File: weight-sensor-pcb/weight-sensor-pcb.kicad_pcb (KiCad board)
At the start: 2 copper layers, 60 parts, among them IC1 SN65HVD230DR, IC2 INA333AIDGKR, IC3 INA333AIDGKR, IC4 INA333AIDGKR, IC5 INA333AIDGKR, IC7 AP63203WU-7, J1 TC2030, J2 54602-908LF, J3 SM04B-GHS-TB_LF__SN_, J4 Conn_01x05_Pin, J5 SM04B-GHS-TB_LF__SN_, J6 SM04B-GHS-TB_LF__SN_, J7 SM04B-GHS-TB_LF__SN_, J8 54602-908LF, J9 10118192-0002LF, Q2 DMP3099L-7, U1 OPA333xxD, U2 OPA333xxD, U3 OPA333xxD, U4 STM32F042F4P6, U5 OPA333xxD

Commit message: layout progress 1
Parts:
- removed R25, R27: 100Ω, Capstone:RESC1608X55N
- added IC6: LM2776DBVR, Capstone:SOT95P280X145-6N, F.Cu at (18.8, 75.5)
- added R18: 0Ω, Capstone:RESC1608X55N, F.Cu at (40.4, 88.7)
- added R4: 0Ω, Capstone:RESC1608X55N, F.Cu at (36.5, 81.0)
- added TP1: VDD, TestPoint:TestPoint_Pad_D1.5mm, F.Cu at (37.0, 99.4)
- added TP10: GND, TestPoint:TestPoint_Pad_D1.5mm, F.Cu at (40.6, 113.6)
- added TP11: CAN_RX, TestPoint:TestPoint_Pad_D1.5mm, F.Cu at (25.9, 99.4)
- added TP12: CAN_TX, TestPoint:TestPoint_Pad_D1.5mm, F.Cu at (25.9, 103.0)
- added TP13: CAN_L, TestPoint:TestPoint_Pad_D1.5mm, F.Cu at (25.9, 106.5)
- added TP14: CAN_H, TestPoint:TestPoint_Pad_D1.5mm, F.Cu at (25.9, 110.0)
- added TP15: RS Mode, TestPoint:TestPoint_Pad_D1.5mm, F.Cu at (25.9, 113.6)
- added TP16: Vref, TestPoint:TestPoint_Pad_D1.5mm, F.Cu at (31.5, 99.4)
- added TP17: V1 OUT, TestPoint:TestPoint_Pad_D1.5mm, F.Cu at (31.5, 103.0)
- added TP18: V2 OUT, TestPoint:TestPoint_Pad_D1.5mm, F.Cu at (31.5, 106.5)
- added TP19: V3 OUT, TestPoint:TestPoint_Pad_D1.5mm, F.Cu at (31.5, 110.0)
- added TP2: BOOT0, TestPoint:TestPoint_Pad_D1.5mm, F.Cu at (115.0, 64.7)
- added TP20: V4 OUT, TestPoint:TestPoint_Pad_D1.5mm, F.Cu at (31.5, 113.6)
- added TP21: SW, TestPoint:TestPoint_Pad_D1.5mm, F.Cu at (104.1, 37.3)
- added TP3: NRST, TestPoint:TestPoint_Pad_D1.5mm, F.Cu at (37.0, 106.5)
- added TP4: VDD, TestPoint:TestPoint_Pad_D1.5mm, F.Cu at (37.0, 110.0)
- added TP5: VDDA, TestPoint:TestPoint_Pad_D1.5mm, F.Cu at (37.0, 113.6)
- added TP6: ADC_IN0, TestPoint:TestPoint_Pad_D1.5mm, F.Cu at (40.6, 99.4)
- added TP7: ADC_IN1, TestPoint:TestPoint_Pad_D1.5mm, F.Cu at (40.6, 103.0)
- added TP8: ADC_IN5, TestPoint:TestPoint_Pad_D1.5mm, F.Cu at (40.6, 106.5)
- added TP9: ADC_IN6, TestPoint:TestPoint_Pad_D1.5mm, F.Cu at (40.6, 110.0)
- R2, R9: value 100Ω -> 0Ω
- moved J8 83.1 mm to (43.6, 29.5), turned to 180 degrees
- moved J2 74.8 mm to (62.0, 29.5), turned to 180 degrees
- moved C13 57.8 mm to (101.0, 40.1), turned to 180 degrees
- moved IC7 55.3 mm to (99.5, 43.6), turned to -90 degrees
- moved L3 55.0 mm to (106.5, 42.6)
- moved Q2 49.5 mm to (94.5, 41.6), turned to 90 degrees
- moved R8 47.1 mm to (117.5, 65.0), turned to 180 degrees
- moved R24 43.7 mm to (94.0, 47.1), turned to 90 degrees
- moved C14 43.5 mm to (98.0, 47.6), turned to 180 degrees
- moved D2 42.8 mm to (95.0, 44.6), turned to 180 degrees
- moved C16 41.3 mm to (102.4, 50.6), turned to 180 degrees
- moved C15 41.0 mm to (102.4, 47.8), turned to 180 degrees
- moved C5 35.1 mm to (108.0, 64.0)
- moved C7 35.1 mm to (108.0, 68.0)
- moved FB1 32.0 mm to (100.9, 55.5)
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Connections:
- net /Power Supply/Input renamed /Power Supply/VIN
- net Net-(IC7-SW) renamed /Power Supply/SW
- net Net-(U1--) renamed /Force Sensor & Analog Front-End/V4out
- net Net-(U2--) renamed /Force Sensor & Analog Front-End/V1out
- net Net-(U3--) renamed /Force Sensor & Analog Front-End/V2out
- net Net-(U5--) renamed /Force Sensor & Analog Front-End/V3out
- IC2 pad 5: GND -> /Force Sensor & Analog Front-End/Vref
- IC3 pad 5: GND -> /Force Sensor & Analog Front-End/Vref
- IC4 pad 5: GND -> /Force Sensor & Analog Front-End/Vref
- IC5 pad 5: GND -> /Force Sensor & Analog Front-End/Vref
- J2 pad 3: unconnected-(J2-Pad3) -> +24V
- J2 pad 4: unconnected-(J2-Pad4) -> GND
- J2 pad 5: unconnected-(J2-Pad5) -> +24V
- J2 pad 6: unconnected-(J2-Pad6) -> GND
- J2 pad 7: unconnected-(J2-Pad7) -> +24V
- J2 pad 8: unconnected-(J2-Pad8) -> GND
- J8 pad 3: unconnected-(J8-Pad3) -> +24V
- J8 pad 4: unconnected-(J8-Pad4) -> GND
- J8 pad 5: unconnected-(J8-Pad5) -> +24V
- J8 pad 6: unconnected-(J8-Pad6) -> GND
- J8 pad 7: unconnected-(J8-Pad7) -> +24V
- J8 pad 8: unconnected-(J8-Pad8) -> GND
- R1 pad 2: Net-(R1-Pad2) -> Net-(IC4-RG_2)
- R2 pad 1: Net-(R1-Pad2) -> Net-(C1-Pad2)
- R2 pad 2: Net-(IC4-RG_2) -> /STM32 Microcontroller/ADC_IN0
- R23 pad 2: Net-(R23-Pad2) -> Net-(IC3-RG_2)
- R26 pad 2: Net-(R26-Pad2) -> Net-(IC2-RG_2)
- R3 pad 2: Net-(R3-Pad2) -> Net-(IC5-RG_2)
- R9 pad 1: Net-(R3-Pad2) -> Net-(C3-Pad2)
- R9 pad 2: Net-(IC5-RG_2) -> /STM32 Microcontroller/ADC_IN5
- U1 pad 3: GND -> /Force Sensor & Analog Front-End/Vref
- U2 pad 3: GND -> /Force Sensor & Analog Front-End/Vref
- U3 pad 3: GND -> /Force Sensor & Analog Front-End/Vref
- U5 pad 3: GND -> /Force Sensor & Analog Front-End/Vref
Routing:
- net +24V: track 0.00 -> 24.3 mm
- net +3.3V: track 1.81 -> 25.5 mm
- net /CAN Interface/CAN_L: track 0.00 -> 19.2 mm
- net /CAN Interface/CAN_H: track 0.00 -> 19.2 mm
- net /Power Supply/SW: track 0.00 -> 13.7 mm
- net /STM32 Microcontroller/NRST: track 0.00 -> 11.2 mm
- net GND: track 1.87 -> 12.3 mm, vias 0 -> 13
- net /STM32 Microcontroller/SWDIO: track 0.00 -> 10.4 mm
- net /STM32 Microcontroller/SWCLK: track 0.00 -> 7.21 mm
- net /Power Supply/VIN: track 0.00 -> 5.56 mm
- net +5V: track 0.00 -> 4.07 mm
- net /STM32 Microcontroller/BOOT0: track 0.00 -> 3.93 mm
- net Net-(IC7-BST): track 0.00 -> 2.57 mm
- net /CAN Interface/RS Mode: track 0.00 -> 1.71 mm
- net /CAN Interface/CAN_RX: track 8.68 -> 7.37 mm
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- added copper zone on F.Cu, net +3.3V
- added copper zone on F.Cu, net /Power Supply/VIN
- added copper zone on B.Cu, net GND

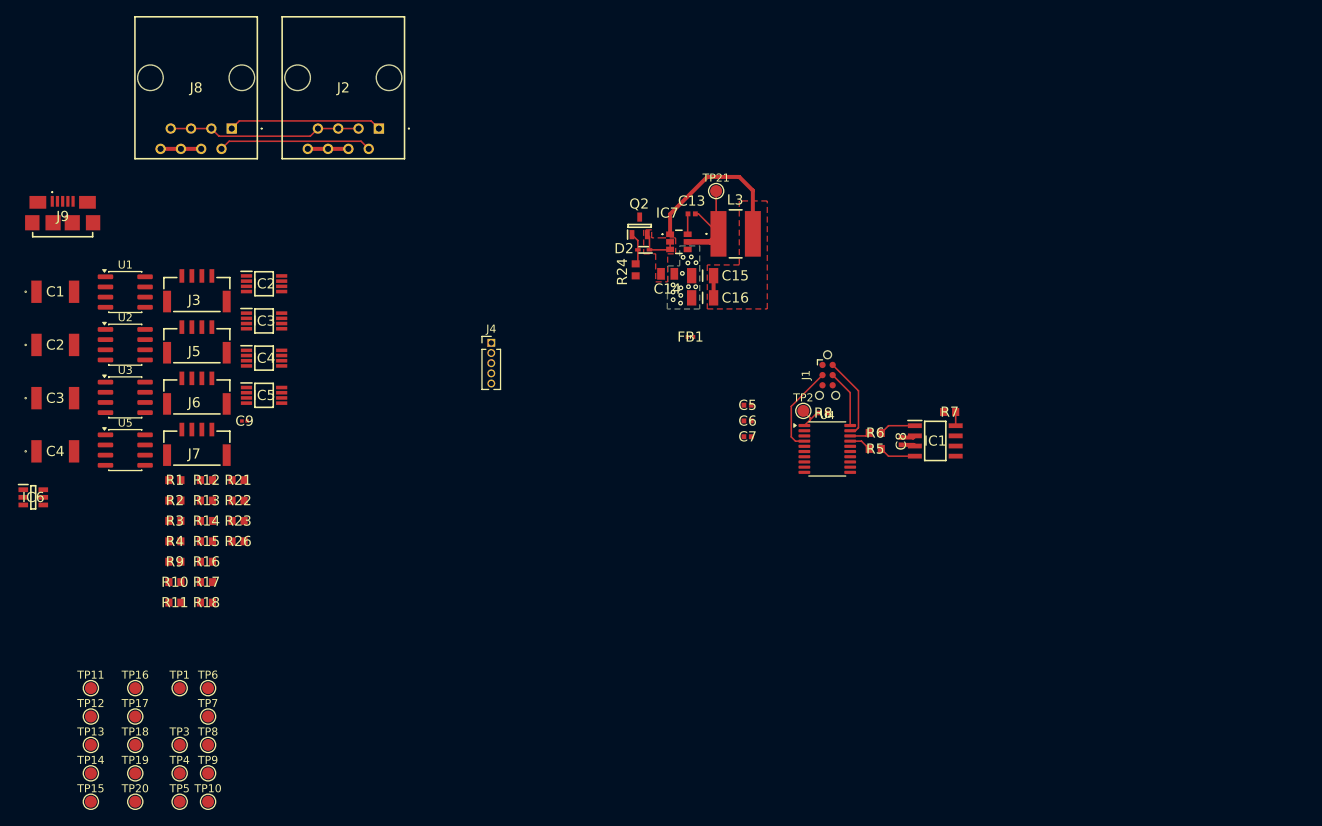
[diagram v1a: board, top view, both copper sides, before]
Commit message: more layout updates, add mounting hole pads to schematic
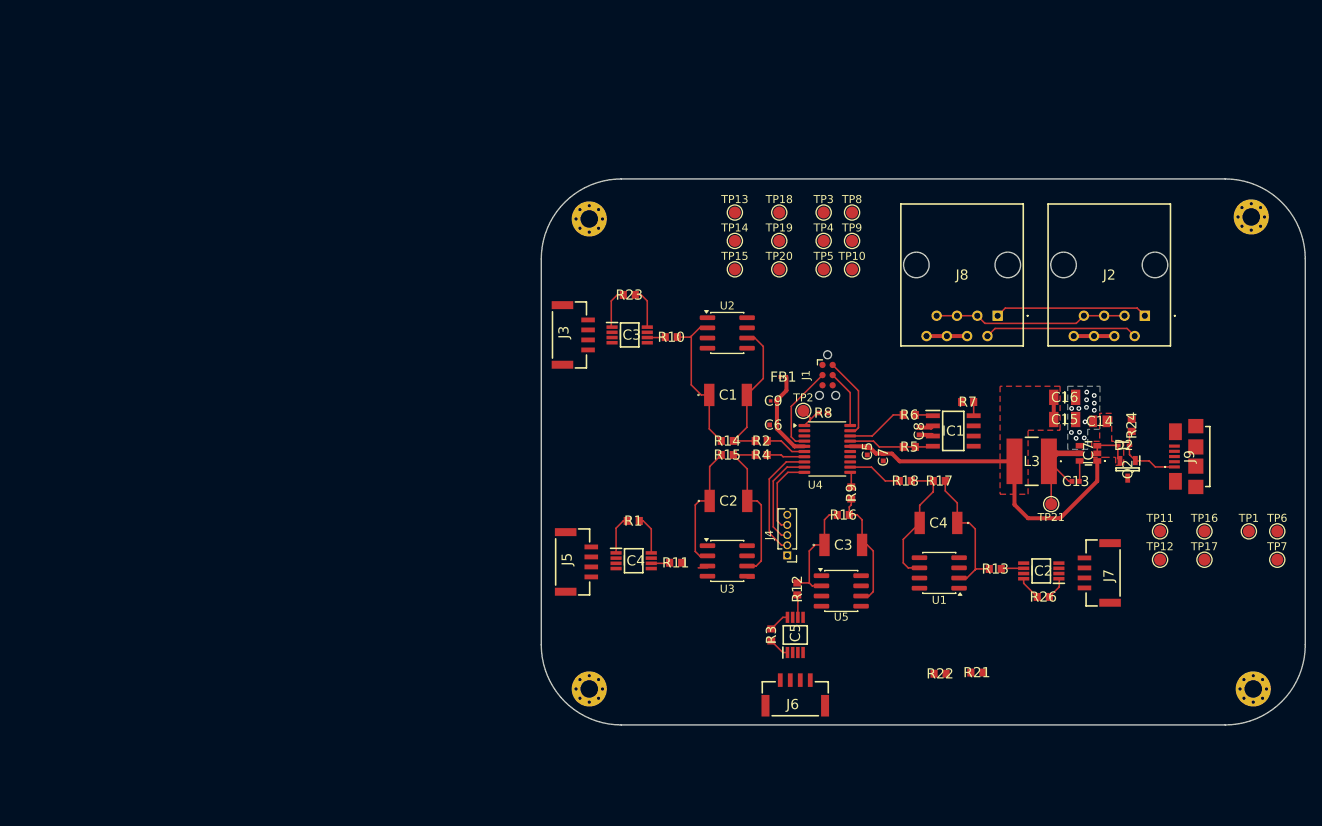
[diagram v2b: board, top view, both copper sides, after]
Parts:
- removed IC6: LM2776DBVR, Capstone:SOT95P280X145-6N
- added H1: MountingHole_Pad, MountingHole:MountingHole_2.2mm_M2_Pad_Via, F.Cu at (88.2, 40.8)
- added H2: MountingHole_Pad, MountingHole:MountingHole_2.2mm_M2_Pad_Via, F.Cu at (171.0, 40.5)
- added H3: MountingHole_Pad, MountingHole:MountingHole_2.2mm_M2_Pad_Via, F.Cu at (171.2, 99.5)
- added H4: MountingHole_Pad, MountingHole:MountingHole_2.2mm_M2_Pad_Via, F.Cu at (88.2, 99.5)
- moved J9 144.0 mm to (163.3, 70.5), turned to 90 degrees
- moved TP11 135.1 mm to (159.6, 79.8)
- moved TP12 135.1 mm to (159.6, 83.3)
- moved TP16 135.1 mm to (165.2, 79.8)
- moved TP17 135.1 mm to (165.2, 83.3)
- moved TP6 135.1 mm to (174.2, 79.8)
- moved TP7 135.1 mm to (174.2, 83.3)
- moved TP1 135.1 mm to (170.7, 79.8)
- moved J7 112.6 mm to (150.3, 85.0), turned to 90 degrees
- moved C4 110.8 mm to (131.9, 78.8), turned to 180 degrees
- moved U1 107.6 mm to (132.0, 85.0), turned to 180 degrees
- moved TP10 104.4 mm to (121.1, 47.0)
- moved TP13 104.4 mm to (106.5, 40.0)
- moved TP14 104.4 mm to (106.5, 43.5)
- moved TP15 104.4 mm to (106.5, 47.0)
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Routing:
- net +3.3V: track 25.5 -> 46.8 mm
- net Net-(C2-Pad2): track 0.00 -> 20.2 mm
- net /Force Sensor & Analog Front-End/V1out: track 0.00 -> 19.5 mm
- net Net-(C1-Pad2): track 0.00 -> 18.6 mm
- net /Force Sensor & Analog Front-End/V4out: track 0.00 -> 17.8 mm
- net Net-(C4-Pad2): track 0.00 -> 16.8 mm
- net /Force Sensor & Analog Front-End/V2out: track 0.00 -> 15.9 mm
- net Net-(C3-Pad2): track 0.00 -> 15.7 mm
- net /STM32 Microcontroller/USART2_TX: track 0.00 -> 14.9 mm
- net /Force Sensor & Analog Front-End/V3out: track 0.00 -> 14.4 mm
- net /STM32 Microcontroller/USART2_RX: track 0.00 -> 12.5 mm
- net +3.3VA: track 0.00 -> 11.5 mm
- net /STM32 Microcontroller/USART2_CK: track 0.00 -> 10.1 mm
- net /STM32 Microcontroller/ADC_IN6: track 0.00 -> 6.85 mm
- net +5V: track 4.07 -> 9.28 mm
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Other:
- board outline added: 95.5 x 68.2 mm

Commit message: Layout draft complete
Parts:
- removed the R21 at (136.7, 97.5)
- removed the R22 at (132.1, 97.6)
- removed the TP1 at (170.7, 79.8)
- removed the TP10 at (121.1, 47.0)
- added C10: 2.2uF, Capstone:CAPC1608X90N, F.Cu at (140.5, 82.3)
- added C11: 2.2uF, Capstone:CAPC1608X90N, F.Cu at (140.5, 84.8)
- added C12: 1uF, Capstone:CAPC1005X70N, F.Cu at (146.1, 83.0)
- added C6: 0.1uF, Capstone:CAPC0603X33N, F.Cu at (139.0, 82.4)
- added IC5: LM2776DBVR, Capstone:SOT95P280X145-6N, F.Cu at (143.4, 83.4)
- added R5: 100Ω, Capstone:RESC1608X55N, F.Cu at (142.9, 94.6)
- added R6: 100Ω, Capstone:RESC1608X55N, F.Cu at (94.8, 52.6)
- added R7: 100Ω, Capstone:RESC1608X55N, F.Cu at (95.3, 80.6)
- added R8: 100Ω, Capstone:RESC1608X55N, F.Cu at (111.0, 91.2)
- moved TP2 70.7 mm to (98.2, 60.8)
- moved TP7 66.6 mm to (109.1, 66.2)
- moved TP8 65.4 mm to (109.7, 72.4)
- moved TP1 47.1 mm to (123.2, 58.4)
- moved TP5 40.9 mm to (133.9, 81.7)
- moved TP20 39.6 mm to (142.7, 59.3)
- moved TP19 38.6 mm to (139.8, 59.4)
- moved TP11 38.3 mm to (137.7, 76.1)
- moved TP18 38.3 mm to (127.5, 62.5)
- moved TP9 35.5 mm to (123.2, 75.4)
- moved TP4 33.6 mm to (116.8, 76.7)
- moved TP21 33.3 mm to (136.5, 61.3)
- moved TP3 31.9 mm to (101.3, 70.0)
- moved TP10 31.2 mm to (128.3, 73.9)
- moved TP17 27.4 mm to (133.1, 73.0)
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- renumbered C4 to C1, C14 to C13, C13 to C14, C16 to C15, C15 to C16, C8 to C17, C1 to C2, C2 to C3, C3 to C4, C9 to C5, C5 to C8, C6 to C9, D2 to D1, IC2 to IC1, IC3 to IC2, IC4 to IC3, IC5 to IC4, IC7 to IC6, IC1 to IC7, J3 to J1, J5 to J2, J6 to J3, J7 to J4, J4 to J5, J1 to J6, J2 to J7, L3 to L1, Q2 to Q1, R26 to R1, R17 to R13, R2 to R17, R4 to R18, R9 to R19, R23 to R2, R18 to R20, R8 to R21, R24 to R22, R7 to R23, R5 to R24, R6 to R25, R1 to R3, R3 to R4, R13 to R9, TP16 to TP1, TP9 to TP10, TP4 to TP11, TP5 to TP12, TP2 to TP14, TP21 to TP16, TP11 to TP17, TP12 to TP18, TP13 to TP19, TP17 to TP2, TP14 to TP20, TP15 to TP21, TP18 to TP3, TP19 to TP4, TP20 to TP5, TP3 to TP6, TP6 to TP7, TP7 to TP8, TP8 to TP9, U5 to U4, U4 to U5
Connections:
- IC1 pad 4: GND -> -3V3
- IC1 pad 5: /Force Sensor & Analog Front-End/Vref -> GND
- IC1 pad 8: Net-(IC2-RG_2) -> Net-(IC1-RG_2)
- IC2 pad 4: GND -> -3V3
- IC2 pad 5: /Force Sensor & Analog Front-End/Vref -> GND
- IC2 pad 8: Net-(IC3-RG_2) -> Net-(IC2-RG_2)
- IC3 pad 4: GND -> -3V3
- IC3 pad 5: /Force Sensor & Analog Front-End/Vref -> GND
- IC3 pad 8: Net-(IC4-RG_2) -> Net-(IC3-RG_2)
- IC4 pad 4: GND -> -3V3
- IC4 pad 5: /Force Sensor & Analog Front-End/Vref -> GND
- IC4 pad 8: Net-(IC5-RG_2) -> Net-(IC4-RG_2)
- J1 pad 2: /Force Sensor & Analog Front-End/V1i+ -> /Force Sensor & Analog Front-End/V1i-
- J1 pad 3: /Force Sensor & Analog Front-End/V1i- -> /Force Sensor & Analog Front-End/V1i+
- J1 pad 4: GND -> -3V3
- J2 pad 2: /Force Sensor & Analog Front-End/V2i+ -> /Force Sensor & Analog Front-End/V2i-
- J2 pad 3: /Force Sensor & Analog Front-End/V2i- -> /Force Sensor & Analog Front-End/V2i+
- J2 pad 4: GND -> -3V3
- J3 pad 2: /Force Sensor & Analog Front-End/V3i+ -> /Force Sensor & Analog Front-End/V3i-
- J3 pad 3: /Force Sensor & Analog Front-End/V3i- -> /Force Sensor & Analog Front-End/V3i+
- J3 pad 4: GND -> -3V3
- J4 pad 2: /Force Sensor & Analog Front-End/V4i+ -> /Force Sensor & Analog Front-End/V4i-
- J4 pad 3: /Force Sensor & Analog Front-End/V4i- -> /Force Sensor & Analog Front-End/V4i+
- J4 pad 4: GND -> -3V3
- R1 pad 2: Net-(IC2-RG_2) -> Net-(R1-Pad2)
- R2 pad 2: Net-(IC3-RG_2) -> Net-(R2-Pad2)
- R3 pad 2: Net-(IC4-RG_2) -> Net-(R3-Pad2)
- R4 pad 2: Net-(IC5-RG_2) -> Net-(R4-Pad2)
- TP1 pad 1: /Force Sensor & Analog Front-End/Vref -> GND
- U1 pad 3: /Force Sensor & Analog Front-End/Vref -> GND
- U1 pad 4: GND -> -3V3
- U2 pad 3: /Force Sensor & Analog Front-End/Vref -> GND
- U2 pad 4: GND -> -3V3
- U3 pad 3: /Force Sensor & Analog Front-End/Vref -> GND
- U3 pad 4: GND -> -3V3
- U4 pad 3: /Force Sensor & Analog Front-End/Vref -> GND
- U4 pad 4: GND -> -3V3
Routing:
- net +3.3VA: track 11.5 -> 184.8 mm, vias 0 -> 5
- net -3V3: track 0.00 -> 158.8 mm, vias 0 -> 8
- net +3.3V: track 46.8 -> 104.4 mm, vias 0 -> 4
- net GND: track 12.3 -> 67.7 mm, vias 13 -> 30
- net /CAN Interface/CAN_H: track 19.2 -> 57.0 mm, vias 0 -> 1
- net +24V: track 24.3 -> 47.0 mm, vias 0 -> 1
- net /CAN Interface/CAN_L: track 19.2 -> 37.5 mm, vias 0 -> 1
- net /Force Sensor & Analog Front-End/V4i+: track 0.00 -> 10.5 mm
- net /Force Sensor & Analog Front-End/V4out: track 17.8 -> 28.1 mm
- net +5V: track 9.28 -> 19.5 mm
- net /Force Sensor & Analog Front-End/V4i-: track 0.00 -> 9.66 mm
- net /Force Sensor & Analog Front-End/V2out: track 15.9 -> 25.6 mm, vias 0 -> 2
- net /Force Sensor & Analog Front-End/V1out: track 19.5 -> 25.4 mm
- net /Force Sensor & Analog Front-End/V3out: track 14.4 -> 19.5 mm
- net /CAN Interface/CAN_RX: track 10.7 -> 15.8 mm
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- added copper zone on F.Cu, net GND
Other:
- board text added: "RX"
- board text added: "TX"
